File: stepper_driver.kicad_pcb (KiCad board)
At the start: 4 copper layers, 56 x 56 mm, 116 parts, among them IC1 TMC2160-TA, J1 BARREL_JACK, J2 Screw_Terminal_01x04, J3 CONN_02X07, J5 Conn_Coaxial, J9 USB_C_Receptacle_USB2.0, Q1 Q_NPN_BEC, Q2 NCE6005AS, Q3 NCE6005AS, Q4 Q_NPN_BEC, Q5 NCE6005AS, Q6 NCE6005AS, SW1 SW_Push, SW2 SW_Push, U1 CH340B, U2 XC6210B332MR, U3 TP6841S6-A, U4 ESP32-PICO-D4, U5 TP6841S6-A

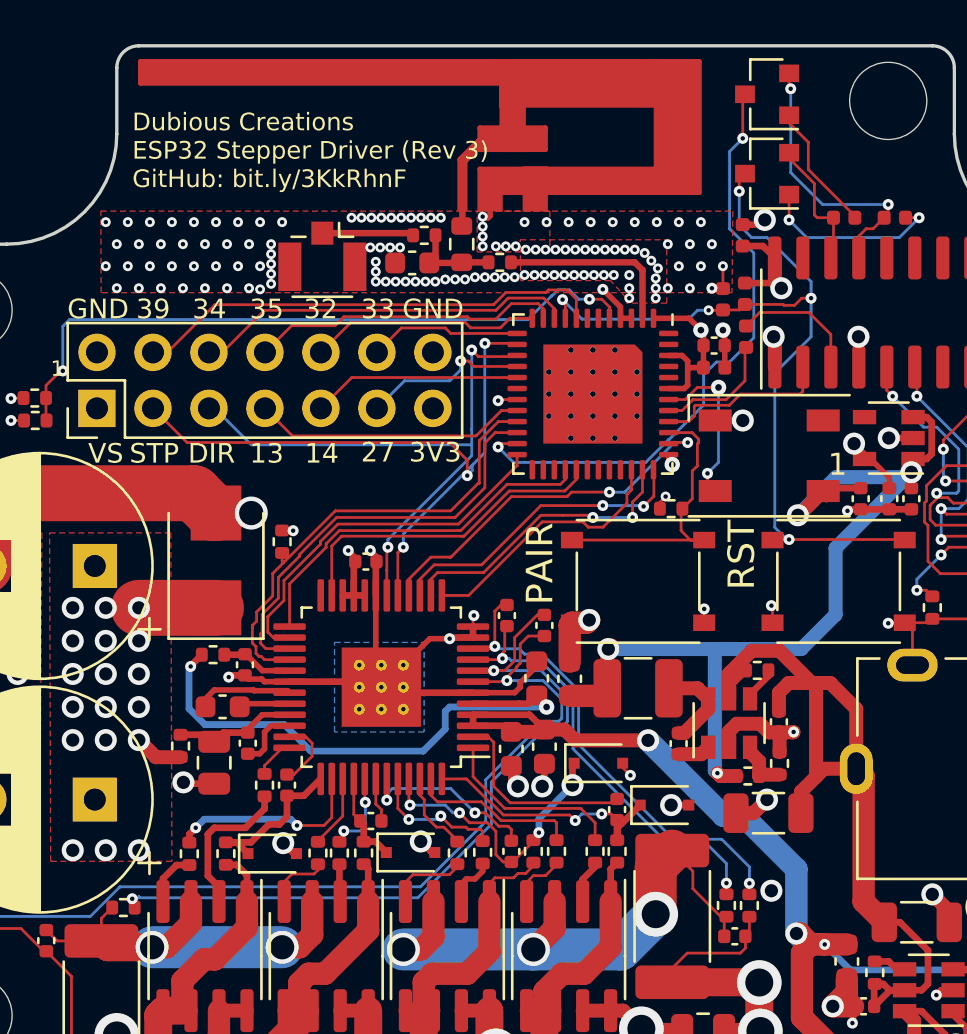
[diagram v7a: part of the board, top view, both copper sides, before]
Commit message: Minor PCB cleanup and updated tline analysis
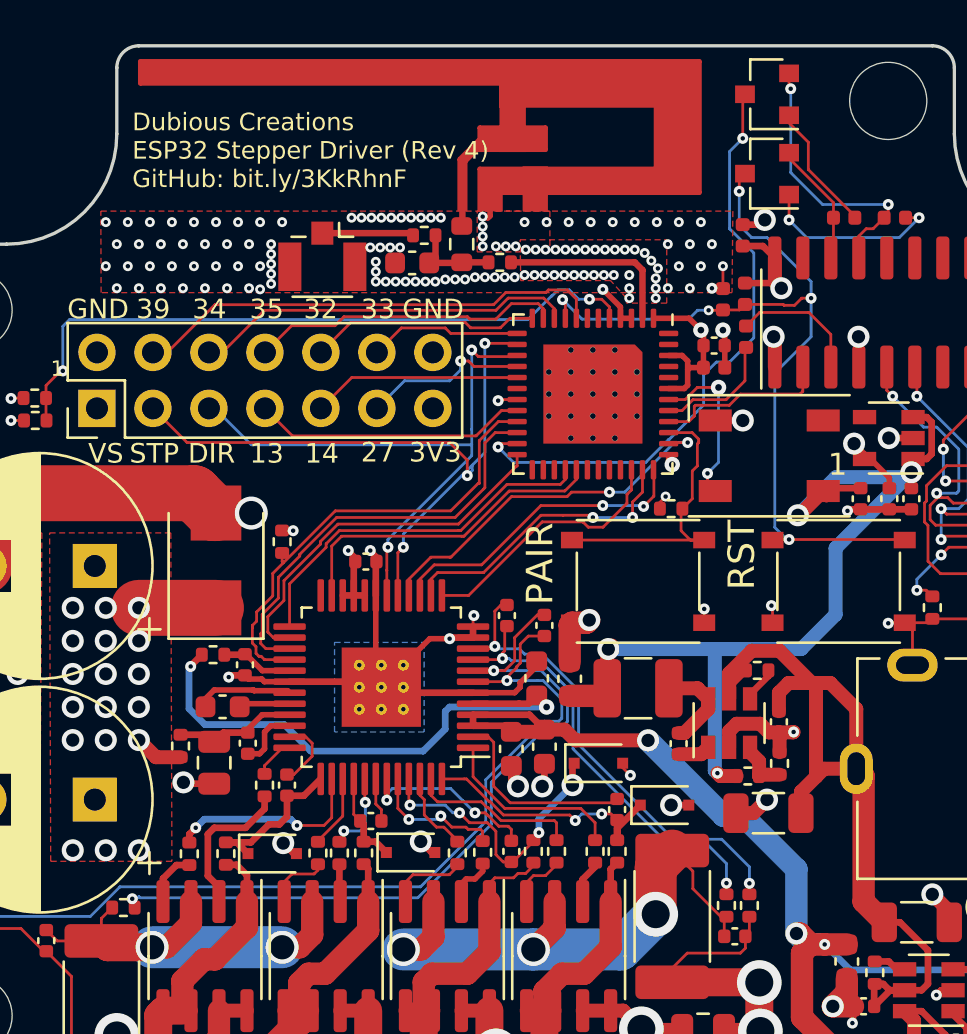
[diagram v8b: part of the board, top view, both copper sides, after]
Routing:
- net GND: vias 182 -> 181
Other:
- board text added: "Dubious Creations ESP32 Stepper Driver (Rev 4) GitHub: bit.ly/3KkRhnF"
- board text removed: "Dubious Creations ESP32 Stepper Driver (Rev 3) GitHub: bit.ly/3KkRhnF"
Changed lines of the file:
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@@
     (thickness 1.6)
     (drawings 54)
-    (tracks 1425)
+    (tracks 1422)
     (zones 0)
     (modules 116)
@@
   )
   (setup
-    (last_trace_width 2.54)
+    (last_trace_width 0.127)
     (user_trace_width 0.127)
     (user_trace_width 0.146812)
@@
     (effects (font (size 0.889 0.889) (thickness 0.15)))
   )
-  (gr_text "Dubious Creations\nESP32 Stepper Driver (Rev 3)\nGitHub: bit.ly/3KkRhnF" (at 132.5 54.55) (layer F.SilkS)
+  (gr_text "Dubious Creations\nESP32 Stepper Driver (Rev 4)\nGitHub: bit.ly/3KkRhnF" (at 132.5 54.55) (layer F.SilkS)
     (effects (font (size 0.8 0.8) (thickness 0.15)) (justify left))
   )
@@
   (segment (start 171.9 63.6) (end 171.8 63.5) (width 0.635) (layer F.Cu) (net 1))
   (segment (start 171.9 64.39) (end 171.9 63.6) (width 0.635) (layer F.Cu) (net 1))
-  (via (at 161.499 88.135496) (size 1) (drill 0.6) (layers F.Cu B.Cu) (net 1))
   (via (at 161.3 84) (size 1) (drill 0.6) (layers F.Cu B.Cu) (net 1))
   (segment (start 160.685 84.615) (end 161.3 84) (width 0.635) (layer F.Cu) (net 1))
@@
   (segment (start 164.315 59.305) (end 164.195 59.425) (width 0.127) (layer F.Cu) (net 4))
   (segment (start 164.315 57.6) (end 164.315 59.305) (width 0.127) (layer F.Cu) (net 4))
+  (segment (start 164.315 56.915) (end 164.315 57.6) (width 0.127) (layer F.Cu) (net 4))
+  (segment (start 162.3 54.9) (end 164.315 56.915) (width 0.127) (layer F.Cu) (net 4))
   (segment (start 162.3 54.65) (end 162.3 54.9) (width 0.127) (layer F.Cu) (net 4))
-  (segment (start 162.3 54.9) (end 163.45 56.05) (width 0.127) (layer F.Cu) (net 4))
-  (segment (start 163.45 56.05) (end 163.45 57.475) (width 0.127) (layer F.Cu) (net 4))
-  (segment (start 163.575 57.6) (end 164.315 57.6) (width 0.127) (layer F.Cu) (net 4))
-  (segment (start 163.45 57.475) (end 163.575 57.6) (width 0.127) (layer F.Cu) (net 4))
   (via (at 162.3 57.7) (size 0.5) (drill 0.2) (layers F.Cu B.Cu) (net 5))
   (via (at 168.2 57.6) (size 0.5) (drill 0.2) (layers F.Cu B.Cu) (net 5))
@@
       )
     )
-  )
-  (zone (net 0) (net_name "") (layer F.Cu) (hatch edge 0.508)
-    (connect_pads (clearance 0.6))
-    (min_thickness 0.254)
-    (keepout (tracks allowed) (vias allowed) (copperpour not_allowed))
-    (fill (arc_segments 32) (thermal_gap 0.508) (thermal_bridge_width 1.5))
-    (polygon
-      (pts
-        (xy 133.17 95.41) (xy 123.01 95.41) (xy 123.01 87.663) (xy 133.17 87.663)
-      )
-    )
